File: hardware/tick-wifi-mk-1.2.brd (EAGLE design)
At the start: 100 x 64 mm, 30 parts, among them IC1 MAX7219, IC2 MAX7219, IC3 74HC125, IC4 LD1117 5V, U1 Adafruit Feather HUZZAH ESP82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

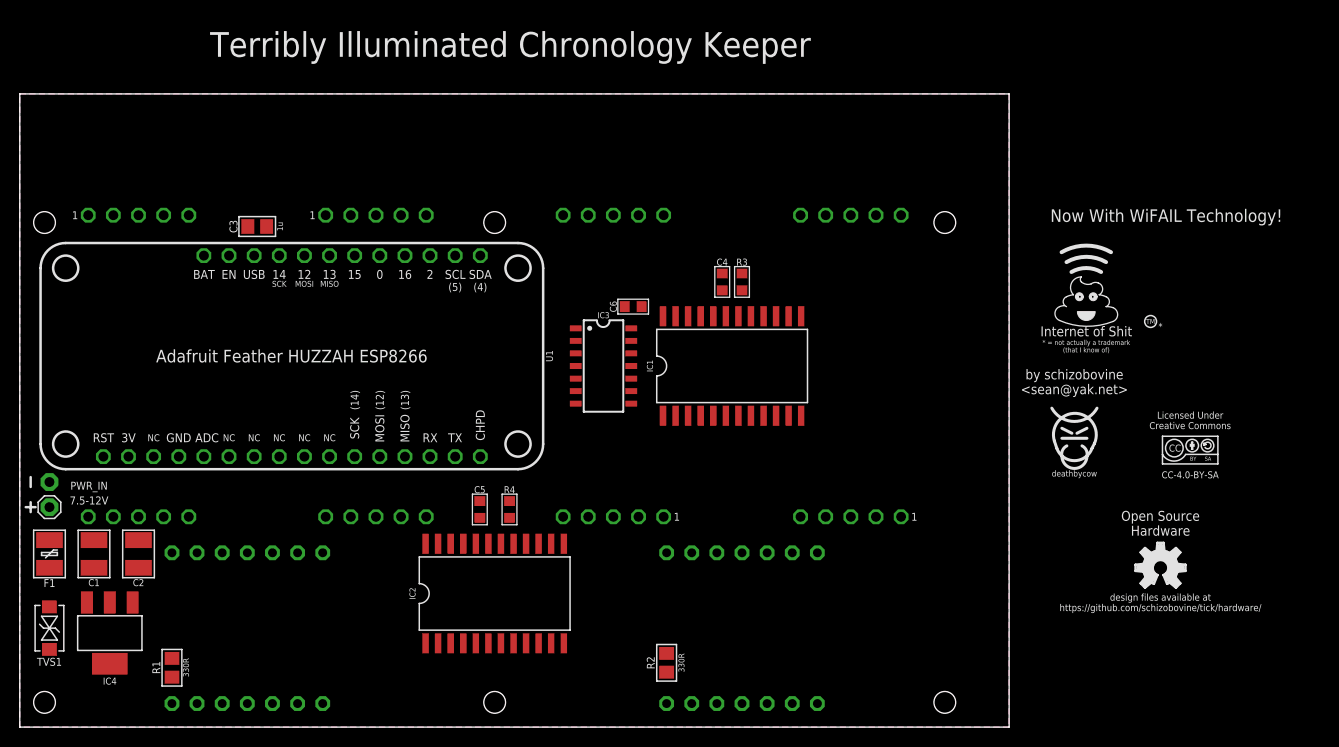
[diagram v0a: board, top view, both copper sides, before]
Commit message: fucking silkscreen error--flipped CLK and DAT markings
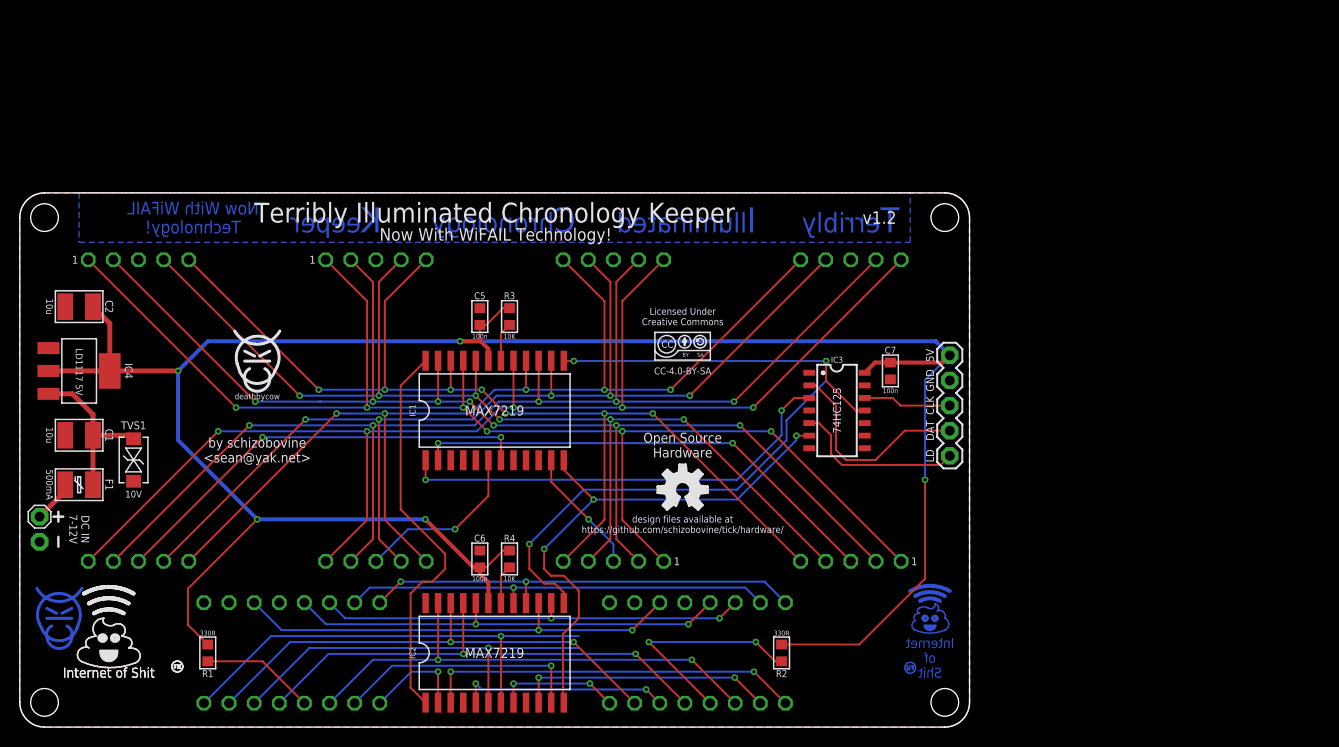
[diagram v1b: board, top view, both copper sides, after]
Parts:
- removed C3: 1u, a_parts:C0805
- removed C4: 100n, a_parts:C0603
- removed PWR_IN: M02PTH-CENTERED-R+, A_butts:1X02-CENTER-R+
- removed U1: Adafruit Feather HUZZAH ESP8266, a_parts:ADAFRUIT_FEATHER_HUZZAH
- added C7: 100n, a_parts:C0603
- added JP1: M05PTH-CENTERED, a_parts:1X05_PTH_CENTERED
- added JP2: M02PTH-CENTERED-R+, a_parts:1X02-CENTER-R+
- added U$10: (no value), a_parts:F_YOU_MARK_METAL
- added U$5: (no value), A_butts:COW_SMALL
- added U$6: (no value), A_butts:CC-BY-SA-4.0-NO-URL
- added U$7: (no value), a_parts:OSHWLOGO_SILKONLY
- added U$9: (no value), a_parts:COW_SMALL_METAL_NOTEXT
- DIGIT1, DIGIT2, DIGIT3, DIGIT4: device A_butts:7SEG_1DIG_25.4MM_NOSILK -> a_parts:7SEG_1DIG_25.4MM_NOSILK
- DISPLAY1, DISPLAY2: value 7SEG_4DIGIT_COLON14.2MM-CC -> 7SEG_4DIGIT_COLON_APOS; device a_parts:7SEG_4DIG_0.56IN_14MM_ADAFRUIT -> a_parts:7SEG_4DIG_10MM
- F1: device A_butts:PTC-1210 -> a_parts:PTC-1210
- FRAME1: device A_butts:DUMMY -> a_parts:DUMMY
- R1, R2: device a_parts:R0805 -> a_parts:R0603
- TVS1: device A_butts:SMA-DIODE-TVS-BIDIR -> a_parts:SMA-DIODE-TVS-BIDIR
- U$1: device A_butts:TICK_SYMBOL -> a_parts:TICK_SYMBOL
- U$2: device A_butts:COW_SMALL -> a_parts:COW_SMALL
- U$3: device a_parts:OSHWLOGO_SILKONLY -> a_parts:INTERNET_OF_SHIT_TEXT_METAL
- U$4: device A_butts:CC-BY-SA-4.0-NO-URL -> a_parts:INTERNET_OF_SHIT_TEXT
- U$8: device a_parts:INTERNET_OF_SHIT -> a_parts:INTERNET_OF_SHIT_JR_METAL
- moved U$4 111.0 mm to (9.00, 8.50)
- moved U$3 106.6 mm to (9.00, 8.50)
- moved U$2 83.0 mm to (24.0, 37.5)
- moved U$8 35.7 mm to (92.0, 11.0), flipped to the bottom
- moved C6 29.8 mm to (46.5, 17.0), turned to 270 degrees
- moved IC4 26.7 mm to (6.00, 36.0), turned to 270 degrees
- moved C2 25.7 mm to (6.00, 42.5), turned to 0 degrees
- moved IC1 24.4 mm to (48.0, 32.0)
- moved IC3 24.0 mm to (82.6, 32.0)
- moved R3 23.8 mm to (49.5, 41.5)
- moved C5 19.5 mm to (46.5, 41.5)
- moved TVS1 19.0 mm to (11.5, 27.0)
- moved C1 12.1 mm to (6.00, 29.5), turned to 180 degrees
- moved R2 11.7 mm to (77.0, 7.50)
- moved F1 7.62 mm to (6.00, 24.5), turned to 0 degrees
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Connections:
- net 5V: now also C6.2, C7.1, JP1.5; no longer C3.1, C4.2, C6.1, U1.USB
- net CTRL_CLCK: now also JP1.3; no longer U1.SCK
- net CTRL_DATA: now also JP1.2; no longer U1.MOSI
- net CTRL_LOAD: now also JP1.1; no longer U1.MISO
- net DIG_1: now also IC1.2; no longer IC1.11
- net DIG_10: now also DISPLAY2.2, IC2.10; no longer DISPLAY2.P$11, IC2.8
- net DIG_11: now also DISPLAY2.6, IC2.5; no longer DISPLAY2.P$10, IC2.10
- net DIG_12: now also DISPLAY2.8, IC2.8; no longer DISPLAY2.P$6, IC2.11
- net DIG_2: now also IC1.11; no longer IC1.6
- net DIG_3: now also IC1.6; no longer IC1.7
- net DIG_4: now also IC1.7; no longer IC1.3
- net DIG_5: now also DISPLAY1.1, IC2.2; no longer DISPLAY1.P$14, IC2.3
- net DIG_6: now also DISPLAY1.2, IC2.11; no longer DISPLAY1.P$11, IC2.5
- net DIG_7: now also DISPLAY1.6; no longer DISPLAY1.P$10
- net DIG_8: now also DISPLAY1.8, IC2.7; no longer DISPLAY1.P$6, IC2.2
- net DIG_9: now also DISPLAY2.1, IC2.3; no longer DISPLAY2.P$14, IC2.7
- net GND: now also C6.1, C7.2, DISPLAY1.12, DISPLAY2.12, JP1.4, JP2.1; no longer C3.2, C4.1, C6.2, DISPLAY1.P$7, DISPLAY2.P$7, PWR_IN.1, U1.GND@0
- net N$1: now also JP2.2; no longer PWR_IN.2
- net N$3: now also DISPLAY1.4; no longer DISPLAY1.P$8
- net N$5: now also DISPLAY2.4; no longer DISPLAY2.P$8
- net SEG_2A: now also DISPLAY1.14, DISPLAY2.14; no longer DISPLAY1.P$13, DISPLAY2.P$13
- net SEG_2B: now also DISPLAY1.16, DISPLAY2.16; no longer DISPLAY1.P$9, DISPLAY2.P$9
- net SEG_2C: now also DISPLAY1.13, DISPLAY2.13; no longer DISPLAY1.P$4, DISPLAY2.P$4
- net SEG_2D: now also DISPLAY1.3, DISPLAY2.3; no longer DISPLAY1.P$2, DISPLAY2.P$2
- net SEG_2E: now also DISPLAY1.5, DISPLAY2.5; no longer DISPLAY1.P$1, DISPLAY2.P$1
- net SEG_2F: now also DISPLAY1.11, DISPLAY2.11; no longer DISPLAY1.P$12, DISPLAY2.P$12
- net SEG_2G: now also DISPLAY1.15, DISPLAY2.15; no longer DISPLAY1.P$5, DISPLAY2.P$5
- net SEG_2P: now also DISPLAY1.7, DISPLAY2.7; no longer DISPLAY1.P$3, DISPLAY2.P$3
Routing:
- net 5V: track 0.00 -> 227.0 mm, vias 0 -> 5
- net SEG_1G: track 0.00 -> 131.1 mm, vias 0 -> 5
- net SEG_1E: track 0.00 -> 131.1 mm, vias 0 -> 6
- net SEG_1D: track 0.00 -> 123.8 mm, vias 0 -> 7
- net SEG_1F: track 0.00 -> 123.8 mm, vias 0 -> 5
- net SEG_1C: track 0.00 -> 113.0 mm, vias 0 -> 6
- net SEG_1A: track 0.00 -> 113.0 mm, vias 0 -> 5
- net SEG_1P: track 0.00 -> 108.9 mm, vias 0 -> 7
- net SEG_1B: track 0.00 -> 108.9 mm, vias 0 -> 5
- net DISP_CLCK: track 0.00 -> 81.7 mm, vias 0 -> 3
- net DISP_LOAD: track 0.00 -> 55.5 mm, vias 0 -> 3
- net SEG_2D: track 0.00 -> 50.4 mm, vias 0 -> 2
- net SEG_2E: track 0.00 -> 50.3 mm, vias 0 -> 2
- net SEG_2P: track 0.00 -> 50.0 mm, vias 0 -> 2
- net DIG_1: track 0.00 -> 48.4 mm, vias 0 -> 2
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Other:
- board size 100 x 64 mm -> 96 x 54 mm
- board text added: "5V"
- board text added: "C"
- board text added: "CLK"
- board text added: "DAT"
- board text added: "DC IN 7-12V"
- board text added: "GND"
- board text added: "I"
- board text added: "K"
- board text added: "LD"
- board text added: "T"
- board text added: "eeper"
- board text added: "erribly"
- board text added: "hronology"
- board text added: "lluminated"
- board text removed: "*"
- board text removed: "* = not actually a trademark (that I know of)"
- board text removed: "7.5-12V"
- board text removed: "TM"
